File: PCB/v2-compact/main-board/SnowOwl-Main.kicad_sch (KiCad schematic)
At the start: 0 parts

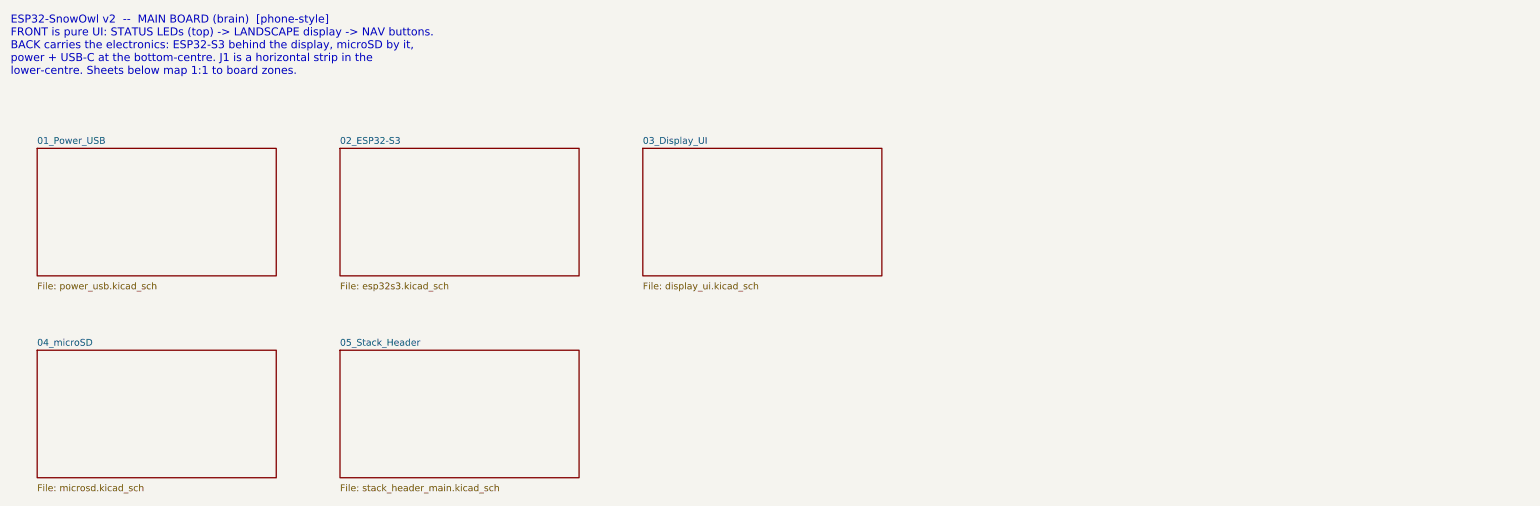
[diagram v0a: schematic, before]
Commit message: Schematics: fix hierarchy load, add verified generator, capture flash sheet
The v2 schematic roots were missing the per-sheet (instances) block, so the
projects would not load in KiCad (kicad-cli failed on both). Regenerate both
roots in a verified format (netlist export now succeeds on both boards).

Populate the first sub-sheet (12_Flash) as the proven pattern: real W25Q128
symbol, decoupling, wired to the SPI spine and power by global labels. Verified
by netlist (U12 pins map to FLASH_CS / SPI_SCK / SPI_MOSI / SPI_MISO / +3V3 / GND).
Remaining sub-sheets to follow the same pattern.
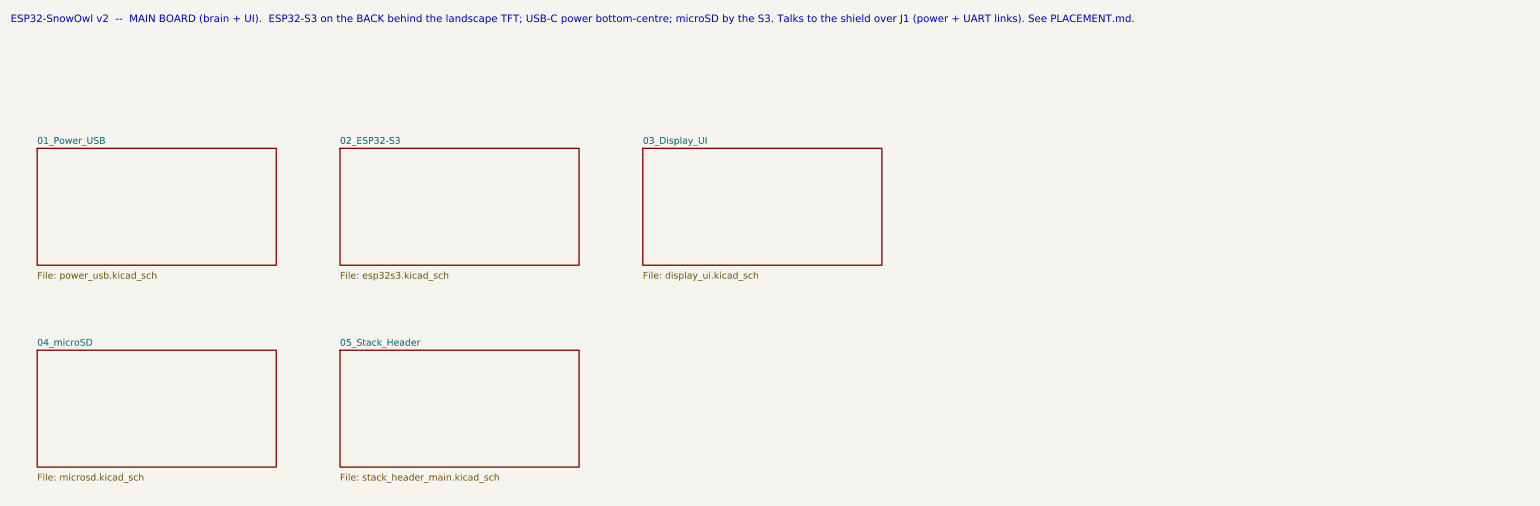
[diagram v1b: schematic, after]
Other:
- note added: "ESP32-SnowOwl v2 -- MAIN BOARD (brain + UI). ESP32-S3 on the BACK behind the landscape TFT; USB-C power bottom-centre; microSD by the S3. Talks to the shield over J1 (power + UART links). See PLACEMENT.md."
- note removed: "ESP32-SnowOwl v2 -- MAIN BOARD (brain) [phone-style] FRONT is pure UI: STATUS LEDs (top) -> LANDSCAPE display -> NAV buttons. BACK carries the electronics: ESP32-S3 behind the display, microSD by it, power + USB-C at the bottom-centre. J1 is a horizontal strip in the lower-centre. Sheets below map 1:1 to board zones."
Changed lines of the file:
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@@
   (title_block (title "SnowOwl v2 - Main Board") (company "YurilLAB")
     (comment 1 "ESP32-SnowOwl v2 - compact 2-board stack"))
-  (text "ESP32-SnowOwl v2  --  MAIN BOARD (brain)  [phone-style]
-FRONT is pure UI: STATUS LEDs (top) -> LANDSCAPE display -> NAV buttons.
-BACK carries the electronics: ESP32-S3 behind the display, microSD by it,
-power + USB-C at the bottom-centre. J1 is a horizontal strip in the
-lower-centre. Sheets below map 1:1 to board zones." (at 20 15 0)
-    (effects (font (size 1.5 1.5)) (justify left top)))
-  (sheet (at 25.0 40.0) (size 45.0 24.0) (fields_autoplaced)
+  (text "ESP32-SnowOwl v2  --  MAIN BOARD (brain + UI).  ESP32-S3 on the BACK behind the landscape TFT; USB-C power bottom-centre; microSD by the S3. Talks to the shield over J1 (power + UART links). See PLACEMENT.md." (at 20 15 0)
+    (effects (font (size 1.4 1.4)) (justify left top)))
+  (sheet (at 25 40) (size 45.0 22.0) (fields_autoplaced)
     (stroke (width 0.1524) (type solid)) (fill (color 0 0 0 0.0000))
-    (property "Sheetname" "01_Power_USB" (at 25.0 39.3 0)
-      (effects (font (size 1.27 1.27)) (justify left bottom)))
-    (property "Sheetfile" "power_usb.kicad_sch" (at 25.0 65.2 0)
-      (effects (font (size 1.27 1.27)) (justify left top)))
+    (property "Sheetname" "01_Power_USB" (at 25 39.3 0) (effects (font (size 1.27 1.27)) (justify left bottom)))
+    (property "Sheetfile" "power_usb.kicad_sch" (at 25 63.2 0) (effects (font (size 1.27 1.27)) (justify left top)))
+    (instances (project "SnowOwl-Main" (path "/a1b2c3d4-0001-4001-8001-000000000001" (page "2"))))
   )
-  (sheet (at 82.0 40.0) (size 45.0 24.0) (fields_autoplaced)
+  (sheet (at 82 40) (size 45.0 22.0) (fields_autoplaced)
     (stroke (width 0.1524) (type solid)) (fill (color 0 0 0 0.0000))
-    (property "Sheetname" "02_ESP32-S3" (at 82.0 39.3 0)
-      (effects (font (size 1.27 1.27)) (justify left bottom)))
-    (property "Sheetfile" "esp32s3.kicad_sch" (at 82.0 65.2 0)
-      (effects (font (size 1.27 1.27)) (justify left top)))
+    (property "Sheetname" "02_ESP32-S3" (at 82 39.3 0) (effects (font (size 1.27 1.27)) (justify left bottom)))
+    (property "Sheetfile" "esp32s3.kicad_sch" (at 82 63.2 0) (effects (font (size 1.27 1.27)) (justify left top)))
+    (instances (project "SnowOwl-Main" (path "/a1b2c3d4-0001-4001-8001-000000000001" (page "3"))))
   )
-  (sheet (at 139.0 40.0) (size 45.0 24.0) (fields_autoplaced)
+  (sheet (at 139 40) (size 45.0 22.0) (fields_autoplaced)
     (stroke (width 0.1524) (type solid)) (fill (color 0 0 0 0.0000))
-    (property "Sheetname" "03_Display_UI" (at 139.0 39.3 0)
-      (effects (font (size 1.27 1.27)) (justify left bottom)))
-    (property "Sheetfile" "display_ui.kicad_sch" (at 139.0 65.2 0)
-      (effects (font (size 1.27 1.27)) (justify left top)))
+    (property "Sheetname" "03_Display_UI" (at 139 39.3 0) (effects (font (size 1.27 1.27)) (justify left bottom)))
+    (property "Sheetfile" "display_ui.kicad_sch" (at 139 63.2 0) (effects (font (size 1.27 1.27)) (justify left top)))
+    (instances (project "SnowOwl-Main" (path "/a1b2c3d4-0001-4001-8001-000000000001" (page "4"))))
   )
-  (sheet (at 25.0 78.0) (size 45.0 24.0) (fields_autoplaced)
+  (sheet (at 25 78) (size 45.0 22.0) (fields_autoplaced)
     (stroke (width 0.1524) (type solid)) (fill (color 0 0 0 0.0000))
-    (property "Sheetname" "04_microSD" (at 25.0 77.3 0)
-      (effects (font (size 1.27 1.27)) (justify left bottom)))
-    (property "Sheetfile" "microsd.kicad_sch" (at 25.0 103.2 0)
-      (effects (font (size 1.27 1.27)) (justify left top)))
+    (property "Sheetname" "04_microSD" (at 25 77.3 0) (effects (font (size 1.27 1.27)) (justify left bottom)))
+    (property "Sheetfile" "microsd.kicad_sch" (at 25 101.2 0) (effects (font (size 1.27 1.27)) (justify left top)))
+    (instances (project "SnowOwl-Main" (path "/a1b2c3d4-0001-4001-8001-000000000001" (page "5"))))
   )
-  (sheet (at 82.0 78.0) (size 45.0 24.0) (fields_autoplaced)
+  (sheet (at 82 78) (size 45.0 22.0) (fields_autoplaced)
     (stroke (width 0.1524) (type solid)) (fill (color 0 0 0 0.0000))
-    (property "Sheetname" "05_Stack_Header" (at 82.0 77.3 0)
-      (effects (font (size 1.27 1.27)) (justify left bottom)))
-    (property "Sheetfile" "stack_header_main.kicad_sch" (at 82.0 103.2 0)
-      (effects (font (size 1.27 1.27)) (justify left top)))
+    (property "Sheetname" "05_Stack_Header" (at 82 77.3 0) (effects (font (size 1.27 1.27)) (justify left bottom)))
+    (property "Sheetfile" "stack_header_main.kicad_sch" (at 82 101.2 0) (effects (font (size 1.27 1.27)) (justify left top)))
+    (instances (project "SnowOwl-Main" (path "/a1b2c3d4-0001-4001-8001-000000000001" (page "6"))))
   )
   (sheet_instances
     (path "/" (page "1"))
-    (path "/5781769a-7303-419b-8493-73073849aff7" (page "2"))
-    (path "/db14e0c1-d42f-42fe-a29f-93976d88e738" (page "3"))
-    (path "/5f352b60-5f6a-4255-98c6-3cd3a1e5b1fb" (page "4"))
-    (path "/c59edb49-d9d8-4ec8-ad65-2bc40d2804a7" (page "5"))
-    (path "/6b0fca45-c8ee-4426-946f-24f4ba9a3d95" (page "6"))
+    (path "/a1b2c3d4-0001-4001-8001-000000000011" (page "2"))
+    (path "/a1b2c3d4-0001-4001-8001-000000000012" (page "3"))
+    (path "/a1b2c3d4-0001-4001-8001-000000000013" (page "4"))
+    (path "/a1b2c3d4-0001-4001-8001-000000000014" (page "5"))
+    (path "/a1b2c3d4-0001-4001-8001-000000000015" (page "6"))
   )
 )
